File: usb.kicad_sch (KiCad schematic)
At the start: 7 parts, among them U501 AMS1117-3.3

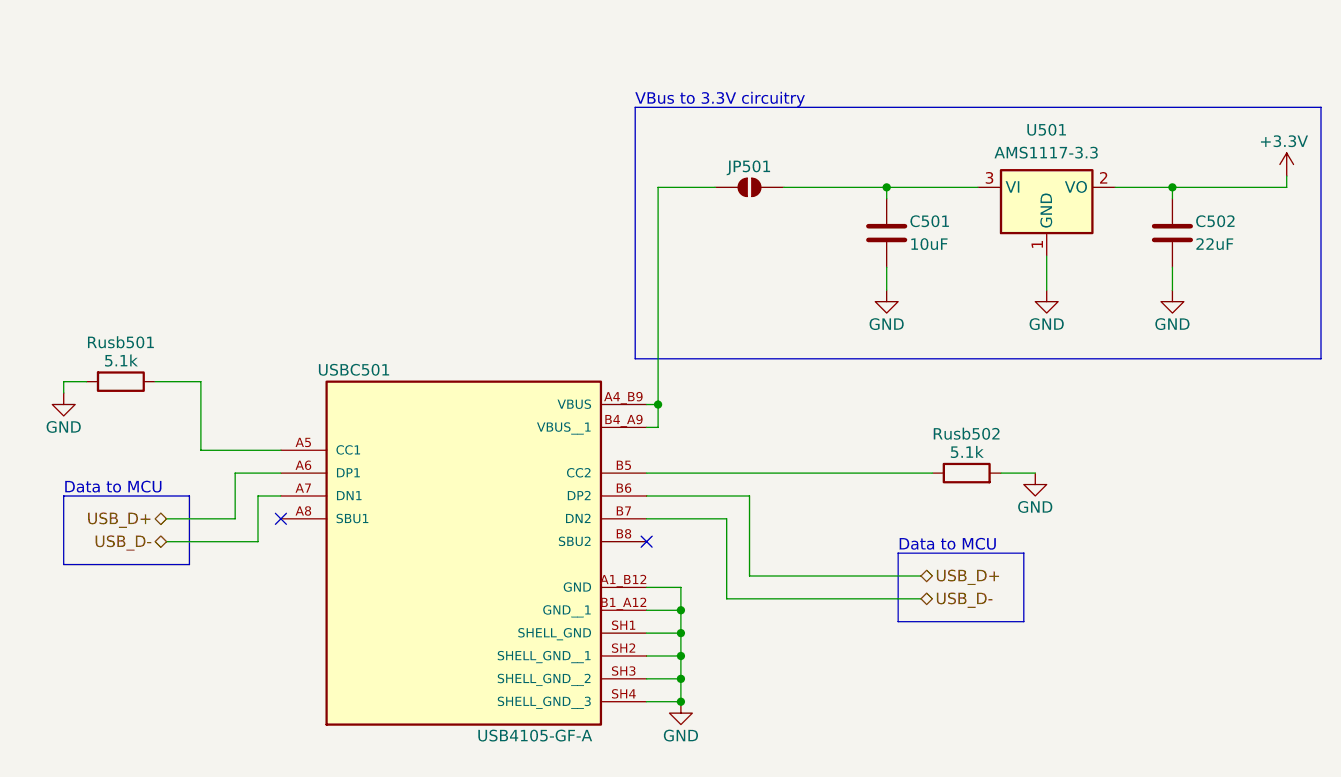
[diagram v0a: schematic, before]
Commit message: Reworked DisplayBoard circuitry and layout; v1.1
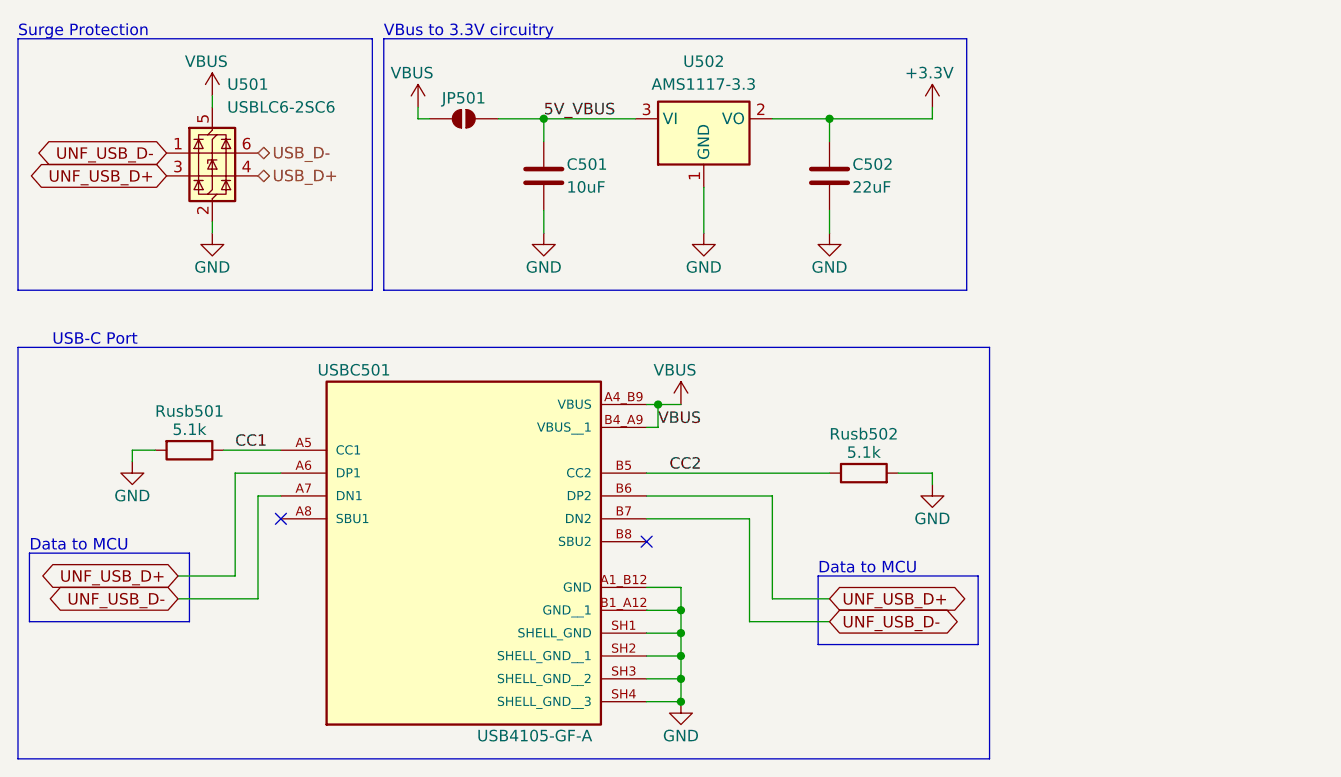
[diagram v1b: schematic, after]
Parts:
- added U501: USBLC6-2SC6, Package_TO_SOT_SMD:SOT-23-6, symbol Power_Protection:USBLC6-2SC6
- renumbered U501 to U502
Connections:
- net GND: now also U501.2 (GND)
- net USB_D+: now also U501.4 (I/O2); no longer USBC501.A6 (DP1), USBC501.B6 (DP2)
- net USB_D-: now also U501.6 (I/O1); no longer USBC501.A7 (DN1), USBC501.B7 (DN2)
- net 5V_VBUS: now reaches C501.1, JP501.2 (B), U502.3 (VI)
- net VBUS: now reaches JP501.1 (A), USBC501.A4_B9 (VBUS), USBC501.B4_A9 (VBUS__1)
- net VBUS: now also U501.5 (VBUS)
- net CC1: now reaches Rusb501.1, USBC501.A5 (CC1)
- net CC2: now reaches Rusb502.1, USBC501.B5 (CC2)
- new net UNF_USB_D+: U501.3 (I/O2), USBC501.A6 (DP1), USBC501.B6 (DP2)
- new net UNF_USB_D-: U501.1 (I/O1), USBC501.A7 (DN1), USBC501.B7 (DN2)
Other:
- note added: "Surge Protection"
- note added: "USB-C Port"
- moved on the sheet: C501, C502, JP501, Rusb501, Rusb502, U502

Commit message: Finished v1.1
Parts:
- renumbered C501 to C14, C502 to C15, JP501 to JP2, Rusb501 to Rusb1, Rusb502 to Rusb2, U501 to U3, U502 to U4, USBC501 to USBC1
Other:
- moved on the sheet: JP2
